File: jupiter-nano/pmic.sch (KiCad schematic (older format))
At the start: 51 parts, among them Q1 BSS138, Q2 BSS138, Q3 BSS138, Q4 BSS138, Q5 BSS138, U2 ACT8945AQJ305-T

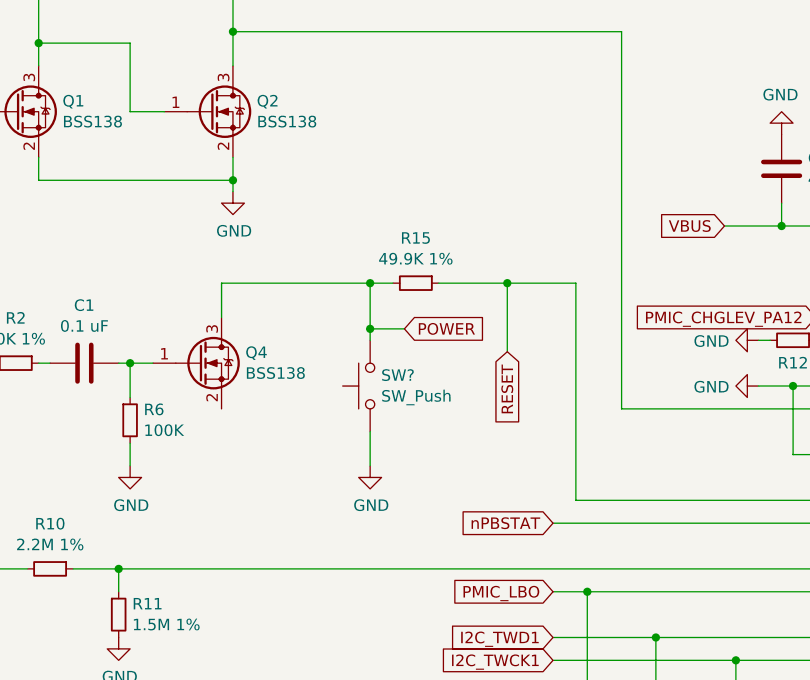
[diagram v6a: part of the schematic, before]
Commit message: reset logic R names, values; longer connnectors
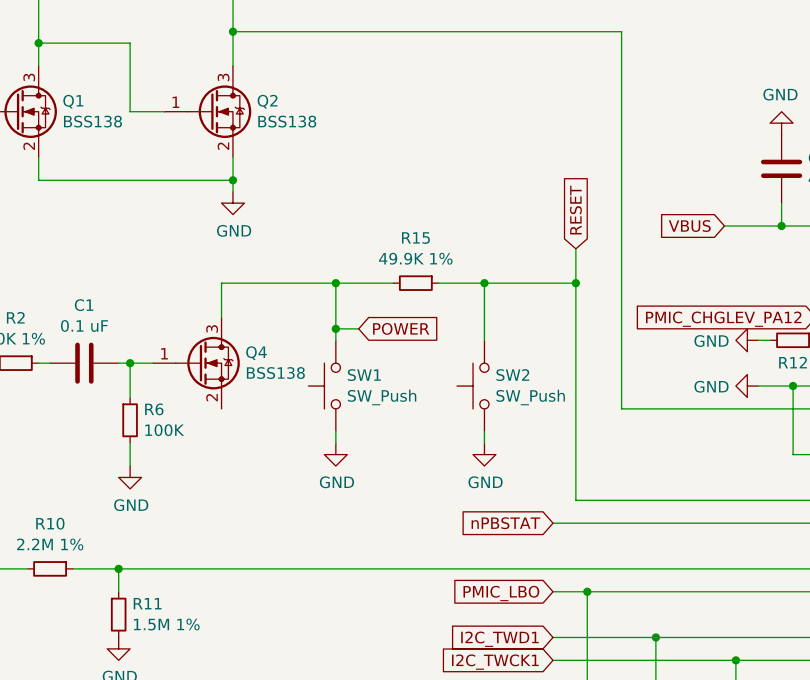
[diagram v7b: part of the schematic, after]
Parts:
- added SW2: SW_Push, symbol Switch:SW_Push
- gave numbers to parts that had none: 1
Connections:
- net GND: now also SW2.1
- net RESET: now also SW2.2
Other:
- moved on the sheet: SW1
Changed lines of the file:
@@
 	5000 2950 3950 2950
 Wire Wire Line
-	3150 2400 3450 2400
-Wire Wire Line
-	3450 2400 3450 2700
-Connection ~ 3450 2400
-Text GLabel 3450 2700 3    50   Input ~ 0
+	3150 2400 3350 2400
+Wire Wire Line
+	3750 2400 3750 2250
+Connection ~ 3750 2400
+Text GLabel 3750 2250 1    50   Input ~ 0
 RESET
 $Comp
-L Switch:SW_Push SW?
+L Switch:SW_Push SW1
 U 1 1 5F7E5404
-P 2850 2850
-F 0 "SW?" V 2896 2802 50  0000 R CNN
-F 1 "SW_Push" V 2805 2802 50  0000 R CNN
-F 2 "" H 2850 3050 50  0001 C CNN
-F 3 "~" H 2850 3050 50  0001 C CNN
-	1    2850 2850
+P 2700 2850
+F 0 "SW1" V 2746 2802 50  0000 R CNN
+F 1 "SW_Push" V 2655 2802 50  0000 R CNN
+F 2 "" H 2700 3050 50  0001 C CNN
+F 3 "~" H 2700 3050 50  0001 C CNN
+	1    2700 2850
 	0    -1   -1   0
 $EndComp
 Wire Wire Line
-	2950 2400 2850 2400
-Wire Wire Line
-	2850 2400 2850 2600
-Wire Wire Line
-	2850 3050 2850 3200
+	2950 2400 2700 2400
+Wire Wire Line
+	2700 2400 2700 2600
+Wire Wire Line
+	2700 3050 2700 3100
 $Comp
 L power:GND #PWR?
 U 1 1 5F8141B2
-P 2850 3200
-F 0 "#PWR?" H 2850 2950 50  0001 C CNN
-F 1 "GND" H 2855 3027 50  0000 C CNN
-F 2 "" H 2850 3200 50  0001 C CNN
-F 3 "" H 2850 3200 50  0001 C CNN
-	1    2850 3200
-	1    0    0    -1
-$EndComp
-Wire Wire Line
-	2850 2600 3000 2600
-Connection ~ 2850 2600
-Wire Wire Line
-	2850 2600 2850 2650
-Text GLabel 3000 2600 2    50   Input ~ 0
+P 2700 3100
+F 0 "#PWR?" H 2700 2850 50  0001 C CNN
+F 1 "GND" H 2705 2927 50  0000 C CNN
+F 2 "" H 2700 3100 50  0001 C CNN
+F 3 "" H 2700 3100 50  0001 C CNN
+	1    2700 3100
+	1    0    0    -1
+$EndComp
+Wire Wire Line
+	2700 2600 2800 2600
+Connection ~ 2700 2600
+Wire Wire Line
+	2700 2600 2700 2650
+Text GLabel 2800 2600 2    50   Input ~ 0
 POWER
 Wire Wire Line
-	2850 2400 2200 2400
+	2700 2400 2200 2400
 Wire Wire Line
 	2200 2400 2200 2550
-Connection ~ 2850 2400
+Connection ~ 2700 2400
 Wire Wire Line
 	1400 2750 1450 2750
@@
 	3750 3350 5000 3350
 Wire Wire Line
-	3450 2400 3750 2400
-Wire Wire Line
 	3950 2950 3950 1300
 Wire Wire Line
@@
 Text GLabel 3650 3950 0    50   Input ~ 0
 I2C_TWD1
+$Comp
+L Switch:SW_Push SW2
+U 1 1 602EB46B
+P 3350 2850
+F 0 "SW2" V 3396 2802 50  0000 R CNN
+F 1 "SW_Push" V 3305 2802 50  0000 R CNN
+F 2 "" H 3350 3050 50  0001 C CNN
+F 3 "~" H 3350 3050 50  0001 C CNN
+	1    3350 2850
+	0    -1   -1   0
+$EndComp
+$Comp
+L power:GND #PWR?
+U 1 1 602EBDEF
+P 3350 3100
+F 0 "#PWR?" H 3350 2850 50  0001 C CNN
+F 1 "GND" H 3355 2927 50  0000 C CNN
+F 2 "" H 3350 3100 50  0001 C CNN
+F 3 "" H 3350 3100 50  0001 C CNN
+	1    3350 3100
+	1    0    0    -1
+$EndComp
+Wire Wire Line
+	3350 3050 3350 3100
+Wire Wire Line
+	3350 2650 3350 2400
+Connection ~ 3350 2400
+Wire Wire Line
+	3350 2400 3750 2400
 $EndSCHEMATC

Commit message: ERC corrections
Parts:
- R16, R18, R22: renamed from R?; value R_Small -> 100K
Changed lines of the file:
@@
 $EndComp
 $Comp
-L power:GND #PWR?
+L power:GND #PWR0142
 U 1 1 5F464585
 P 4650 1750
-F 0 "#PWR?" H 4650 1500 50  0001 C CNN
+F 0 "#PWR0142" H 4650 1500 50  0001 C CNN
 F 1 "GND" H 4655 1577 50  0000 C CNN
 F 2 "" H 4650 1750 50  0001 C CNN
@@
 $EndComp
 $Comp
-L power:GND #PWR?
+L power:GND #PWR0143
 U 1 1 5F467E51
 P 1750 3950
-F 0 "#PWR?" H 1750 3700 50  0001 C CNN
+F 0 "#PWR0143" H 1750 3700 50  0001 C CNN
 F 1 "GND" H 1755 3777 50  0000 C CNN
 F 2 "" H 1750 3950 50  0001 C CNN
@@
 	7750 1700 8000 1700
 $Comp
-L power:GND #PWR?
+L power:GND #PWR0144
 U 1 1 5F4753C7
 P 8000 1700
-F 0 "#PWR?" H 8000 1450 50  0001 C CNN
+F 0 "#PWR0144" H 8000 1450 50  0001 C CNN
 F 1 "GND" H 8005 1527 50  0000 C CNN
 F 2 "" H 8000 1700 50  0001 C CNN
@@
 VBAT
 $Comp
-L power:GND #PWR?
+L power:GND #PWR0145
 U 1 1 5F4885B5
 P 8200 1950
-F 0 "#PWR?" H 8200 1700 50  0001 C CNN
+F 0 "#PWR0145" H 8200 1700 50  0001 C CNN
 F 1 "GND" H 8205 1777 50  0000 C CNN
 F 2 "" H 8200 1950 50  0001 C CNN
@@
 	6400 2450 7050 2450
 $Comp
-L power:GND #PWR?
+L power:GND #PWR0146
 U 1 1 5F495460
 P 7250 2450
-F 0 "#PWR?" H 7250 2200 50  0001 C CNN
+F 0 "#PWR0146" H 7250 2200 50  0001 C CNN
 F 1 "GND" V 7255 2322 50  0000 R CNN
 F 2 "" H 7250 2450 50  0001 C CNN
@@
 	9200 3550 9450 3550
 $Comp
-L power:GND #PWR?
+L power:GND #PWR0147
 U 1 1 5F4B366C
 P 9450 3550
-F 0 "#PWR?" H 9450 3300 50  0001 C CNN
+F 0 "#PWR0147" H 9450 3300 50  0001 C CNN
 F 1 "GND" V 9455 3422 50  0000 R CNN
 F 2 "" H 9450 3550 50  0001 C CNN
@@
 $EndComp
 $Comp
-L power:GND #PWR?
+L power:GND #PWR0148
 U 1 1 5F4B66A9
 P 9450 3950
-F 0 "#PWR?" H 9450 3700 50  0001 C CNN
+F 0 "#PWR0148" H 9450 3700 50  0001 C CNN
 F 1 "GND" V 9455 3822 50  0000 R CNN
 F 2 "" H 9450 3950 50  0001 C CNN
@@
 $EndComp
 $Comp
-L power:GND #PWR?
+L power:GND #PWR0149
 U 1 1 5F4BD37E
 P 9450 4350
-F 0 "#PWR?" H 9450 4100 50  0001 C CNN
+F 0 "#PWR0149" H 9450 4100 50  0001 C CNN
 F 1 "GND" V 9455 4222 50  0000 R CNN
 F 2 "" H 9450 4350 50  0001 C CNN
@@
 	9250 5200 9500 5200
 $Comp
-L power:GND #PWR?
+L power:GND #PWR0150
 U 1 1 5F4DAC88
 P 9500 5200
-F 0 "#PWR?" H 9500 4950 50  0001 C CNN
+F 0 "#PWR0150" H 9500 4950 50  0001 C CNN
 F 1 "GND" H 9505 5027 50  0000 C CNN
 F 2 "" H 9500 5200 50  0001 C CNN
@@
 	6700 4900 6700 4950
 $Comp
-L power:GND #PWR?
+L power:GND #PWR0151
 U 1 1 5F55E012
 P 6850 4900
-F 0 "#PWR?" H 6850 4650 50  0001 C CNN
+F 0 "#PWR0151" H 6850 4650 50  0001 C CNN
 F 1 "GND" V 6855 4772 50  0000 R CNN
 F 2 "" H 6850 4900 50  0001 C CNN
@@
 	4950 4850 4950 5000
 $Comp
-L power:GND #PWR?
+L power:GND #PWR0152
 U 1 1 5F57CB94
 P 4950 5000
-F 0 "#PWR?" H 4950 4750 50  0001 C CNN
+F 0 "#PWR0152" H 4950 4750 50  0001 C CNN
 F 1 "GND" H 4955 4827 50  0000 C CNN
 F 2 "" H 4950 5000 50  0001 C CNN
@@
 	4450 4800 4450 5000
 $Comp
-L power:GND #PWR?
+L power:GND #PWR0153
 U 1 1 5F5E58C5
 P 4100 5000
-F 0 "#PWR?" H 4100 4750 50  0001 C CNN
+F 0 "#PWR0153" H 4100 4750 50  0001 C CNN
 F 1 "GND" H 4105 4827 50  0000 C CNN
 F 2 "" H 4100 5000 50  0001 C CNN
@@
 $EndComp
 $Comp
-L power:GND #PWR?
+L power:GND #PWR0154
 U 1 1 5F5E6EDB
 P 4450 5000
-F 0 "#PWR?" H 4450 4750 50  0001 C CNN
+F 0 "#PWR0154" H 4450 4750 50  0001 C CNN
 F 1 "GND" H 4455 4827 50  0000 C CNN
 F 2 "" H 4450 5000 50  0001 C CNN
@@
 	3800 4800 3800 5000
 $Comp
-L power:GND #PWR?
+L power:GND #PWR0155
 U 1 1 5F60CEF0
 P 3800 5000
-F 0 "#PWR?" H 3800 4750 50  0001 C CNN
+F 0 "#PWR0155" H 3800 4750 50  0001 C CNN
 F 1 "GND" H 3805 4827 50  0000 C CNN
 F 2 "" H 3800 5000 50  0001 C CNN
@@
 Connection ~ 4700 2850
 $Comp
-L power:GND #PWR?
+L power:GND #PWR0156
 U 1 1 5F61A7E3
 P 4550 2850
-F 0 "#PWR?" H 4550 2600 50  0001 C CNN
+F 0 "#PWR0156" H 4550 2600 50  0001 C CNN
 F 1 "GND" V 4555 2722 50  0000 R CNN
 F 2 "" H 4550 2850 50  0001 C CNN
@@
 	4600 2650 4550 2650
 $Comp
-L power:GND #PWR?
+L power:GND #PWR0157
 U 1 1 5F656E22
 P 4550 2650
-F 0 "#PWR?" H 4550 2400 50  0001 C CNN
+F 0 "#PWR0157" H 4550 2400 50  0001 C CNN
 F 1 "GND" V 4555 2522 50  0000 R CNN
 F 2 "" H 4550 2650 50  0001 C CNN
@@
 	2200 7100 2200 7200
 $Comp
-L power:GND #PWR?
+L power:GND #PWR0158
 U 1 1 5F6CBF6E
 P 2200 7200
-F 0 "#PWR?" H 2200 6950 50  0001 C CNN
+F 0 "#PWR0158" H 2200 6950 50  0001 C CNN
 F 1 "GND" H 2205 7027 50  0000 C CNN
 F 2 "" H 2200 7200 50  0001 C CNN
@@
 $EndComp
 $Comp
-L power:GND #PWR?
+L power:GND #PWR0159
 U 1 1 5F6CCAD6
 P 3200 7200
-F 0 "#PWR?" H 3200 6950 50  0001 C CNN
+F 0 "#PWR0159" H 3200 6950 50  0001 C CNN
 F 1 "GND" H 3205 7027 50  0000 C CNN
 F 2 "" H 3200 7200 50  0001 C CNN
@@
 VDDBU
 $Comp
-L Device:R_Small R?
+L Device:R_Small R22
 U 1 1 5F7027C3
 P 3650 6300
-F 0 "R?" H 3709 6346 50  0000 L CNN
-F 1 "R_Small" H 3709 6255 50  0000 L CNN
+F 0 "R22" H 3709 6346 50  0000 L CNN
+F 1 "100K" H 3709 6255 50  0000 L CNN
 F 2 "" H 3650 6300 50  0001 C CNN
 F 3 "~" H 3650 6300 50  0001 C CNN
@@
 $EndComp
 $Comp
-L Device:R_Small R?
+L Device:R_Small R18
 U 1 1 5F70325F
 P 3200 6300
-F 0 "R?" H 3259 6346 50  0000 L CNN
-F 1 "R_Small" H 3259 6255 50  0000 L CNN
+F 0 "R18" H 3259 6346 50  0000 L CNN
+F 1 "100K" H 3259 6255 50  0000 L CNN
 F 2 "" H 3200 6300 50  0001 C CNN
 F 3 "~" H 3200 6300 50  0001 C CNN
@@
 $EndComp
 $Comp
-L Device:R_Small R?
+L Device:R_Small R16
 U 1 1 5F703D5F
 P 2200 6300
-F 0 "R?" H 2259 6346 50  0000 L CNN
-F 1 "R_Small" H 2259 6255 50  0000 L CNN
+F 0 "R16" H 2259 6346 50  0000 L CNN
+F 1 "100K" H 2259 6255 50  0000 L CNN
 F 2 "" H 2200 6300 50  0001 C CNN
 F 3 "~" H 2200 6300 50  0001 C CNN
@@
 	2700 3050 2700 3100
 $Comp
-L power:GND #PWR?
+L power:GND #PWR0160
 U 1 1 5F8141B2
 P 2700 3100
-F 0 "#PWR?" H 2700 2850 50  0001 C CNN
+F 0 "#PWR0160" H 2700 2850 50  0001 C CNN
 F 1 "GND" H 2705 2927 50  0000 C CNN
 F 2 "" H 2700 3100 50  0001 C CNN
@@
 	1800 3100 1800 3200
 $Comp
-L power:GND #PWR?
+L power:GND #PWR0161
 U 1 1 5F85C54C
 P 1800 3200
-F 0 "#PWR?" H 1800 2950 50  0001 C CNN
+F 0 "#PWR0161" H 1800 2950 50  0001 C CNN
 F 1 "GND" H 1805 3027 50  0000 C CNN
 F 2 "" H 1800 3200 50  0001 C CNN
@@
 Connection ~ 2250 1950
 $Comp
-L power:GND #PWR?
+L power:GND #PWR0162
 U 1 1 5F8990CB
 P 2250 2000
-F 0 "#PWR?" H 2250 1750 50  0001 C CNN
+F 0 "#PWR0162" H 2250 1750 50  0001 C CNN
 F 1 "GND" H 2255 1827 50  0000 C CNN
 F 2 "" H 2250 2000 50  0001 C CNN
@@
 $EndComp
 $Comp
-L power:GND #PWR?
+L power:GND #PWR0163
 U 1 1 602EBDEF
 P 3350 3100
-F 0 "#PWR?" H 3350 2850 50  0001 C CNN
+F 0 "#PWR0163" H 3350 2850 50  0001 C CNN
 F 1 "GND" H 3355 2927 50  0000 C CNN
 F 2 "" H 3350 3100 50  0001 C CNN
